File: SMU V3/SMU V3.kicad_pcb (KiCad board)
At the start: 4 copper layers, 55.5 x 74.8 mm, 86 parts, among them J1 Connector, J2 Connector, J3 SMA, J4 SMA, Q1 SI2301CDS-T1-GE3, U1 LSM6DSOTR, U2 TPS7A2033PDBVR, U3 TPS7A2033PDBVR, U4 TPS7A2033PDBVR, U5 ETQ-P3M150KVN, U6 TPS5430DDAR, U7 AMS1117-3.3

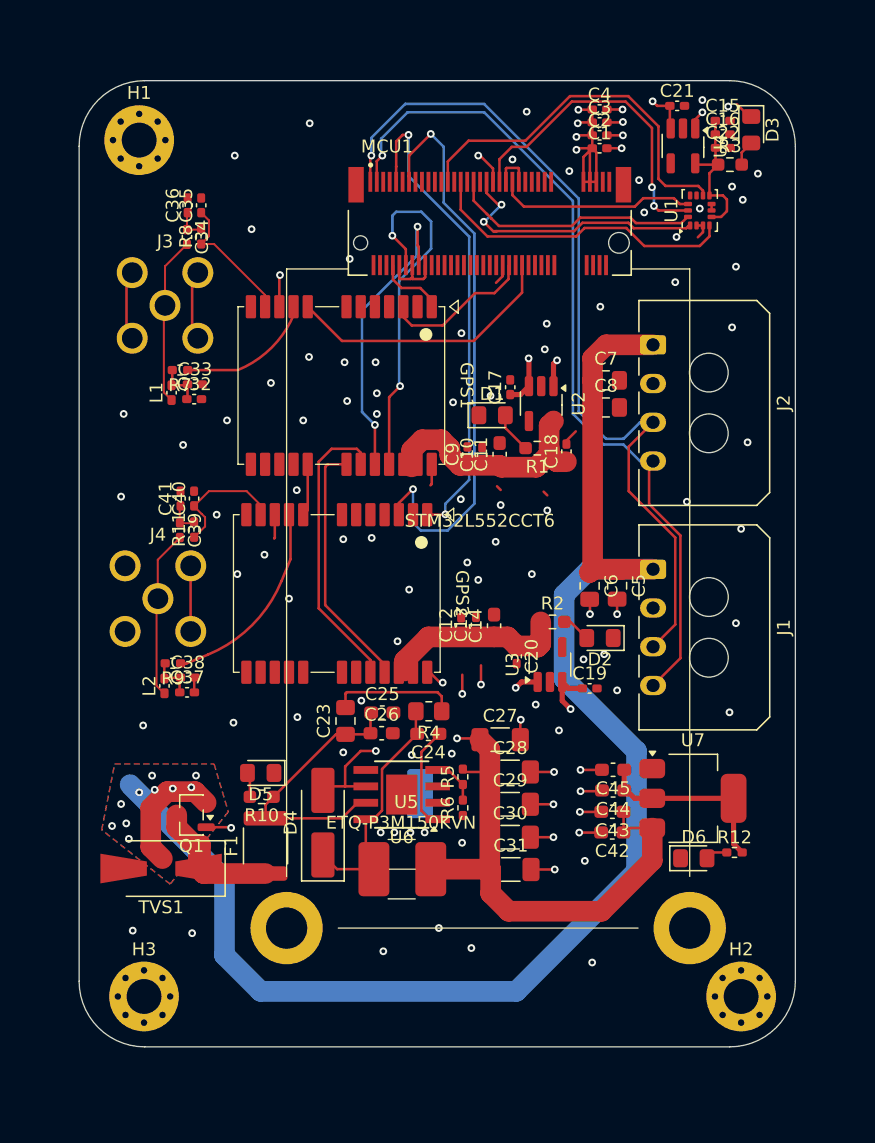
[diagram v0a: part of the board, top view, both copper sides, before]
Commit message: improved V3
added uart/spi test points and status leds
removed main 3v3 ldo
added silkscreen
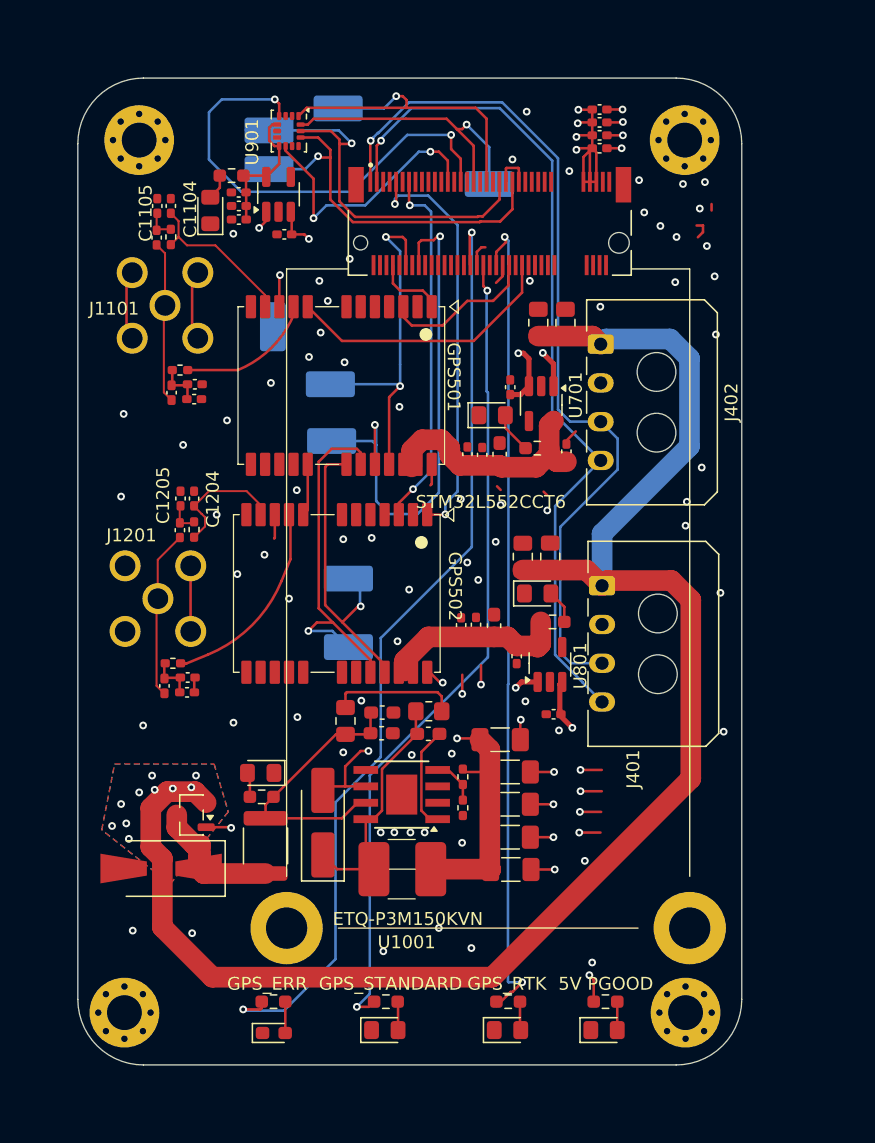
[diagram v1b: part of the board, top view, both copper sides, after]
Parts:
- removed C42, C43, C44, C45: 10u, Capacitor_SMD:C_0603_1608Metric_Pad1.08x0.95mm_HandSolder
- removed D6: Green, Diode_SMD:D_0805_2012Metric_Pad1.15x1.40mm_HandSolder
- removed R12: 220, Resistor_SMD:R_0402_1005Metric_Pad0.72x0.64mm_HandSolder
- removed U7: AMS1117-3.3, Package_TO_SOT_SMD:SOT-223-3_TabPin2
- added D101: Green, Diode_SMD:D_0805_2012Metric_Pad1.15x1.40mm_HandSolder, F.Cu at (165.1, 128.1)
- added D201: Green, Diode_SMD:D_0805_2012Metric_Pad1.15x1.40mm_HandSolder, F.Cu at (157.6, 128.1)
- added D202: Yellow, Diode_SMD:D_0805_2012Metric_Pad1.15x1.40mm_HandSolder, F.Cu at (148.1, 128.1)
- added D203: Red, Diode_SMD:D_0603_1608Metric_Pad1.05x0.95mm_HandSolder, F.Cu at (139.5, 128.3)
- added G***: LOGO, bfr_logos:BFR_Small, B.Cu at (134.6, 105.9)
- added G***: LOGO, images:smu_qrCode, B.Cu at (156.3, 117.3)
- added G***: LOGO, images:sleepingBubu_v2, B.Cu at (156.6, 83.6)
- added H104: MountingHole_Pad_MP, MountingHole:MountingHole_2.7mm_M2.5_Pad_Via, F.Cu at (171.3, 59.2)
- added R101: 120, Resistor_SMD:R_0603_1608Metric_Pad0.98x0.95mm_HandSolder, F.Cu at (165.2, 125.9)
- added R201: 120, Resistor_SMD:R_0603_1608Metric_Pad0.98x0.95mm_HandSolder, F.Cu at (157.7, 125.9)
- added R202: 120, Resistor_SMD:R_0603_1608Metric_Pad0.98x0.95mm_HandSolder, F.Cu at (148.2, 125.9)
- added R203: 120, Resistor_SMD:R_0603_1608Metric_Pad0.98x0.95mm_HandSolder, F.Cu at (139.5, 125.9)
- added TP501: GPS1_UART_RX, bfr_utilities:TestPoint_Keystone_5019_Miniature, B.Cu at (143.9, 78.1)
- added TP502: GPS1_UART_TX, bfr_utilities:TestPoint_Keystone_5019_Miniature, B.Cu at (144.0, 82.5)
- added TP503: GPS2_UART_RX, bfr_utilities:TestPoint_Keystone_5019_Miniature, B.Cu at (145.3, 93.2)
- added TP504: GPS2_UART_TX, bfr_utilities:TestPoint_Keystone_5019_Miniature, B.Cu at (145.3, 98.5)
- added TP601: IMU_SPI_CS, bfr_utilities:TestPoint_Keystone_5019_Miniature, B.Cu at (139.2, 61.5)
- added TP602: IMU_SPI_MISO, bfr_utilities:TestPoint_Keystone_5019_Miniature, B.Cu at (144.5, 56.8)
- added TP603: IMU_SPI_MOSI, bfr_utilities:TestPoint_Keystone_5019_Miniature, B.Cu at (156.2, 62.6)
- added TP604: IMU_SPI_SCK, bfr_utilities:TestPoint_Keystone_5019_Miniature, B.Cu at (139.2, 58.5)
- moved D901 42.3 mm to (134.6, 64.7), turned to 90 degrees
- moved R901 38.6 mm to (136.3, 62.0), turned to 180 degrees
- moved C601 38.2 mm to (136.8, 65.3), turned to 180 degrees
- moved TP301 37.9 mm to (139.4, 73.7)
- moved C602 37.9 mm to (136.8, 64.3), turned to 180 degrees
- moved C902 37.6 mm to (136.8, 63.2), turned to 180 degrees
- moved U601 32.4 mm to (140.7, 58.5), turned to -90 degrees
- moved C901 32.0 mm to (140.3, 66.5), turned to 180 degrees
- moved U901 31.5 mm to (139.9, 63.4), turned to 90 degrees
- moved C401 7.64 mm to (158.8, 91.5), turned to 90 degrees
- moved C404 7.28 mm to (162.1, 73.3), turned to 90 degrees
- moved C403 6.88 mm to (160.0, 73.3), turned to 90 degrees
- moved D801 5.93 mm to (159.9, 94.3), turned to 0 degrees
- moved H102 4.48 mm to (171.4, 126.8)
- moved J401 4.15 mm to (164.9, 93.7)
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- renumbered C23 to C1001, C24 to C1002, C25 to C1003, C26 to C1004, C27 to C1005, C28 to C1006, C29 to C1007, C30 to C1008, C31 to C1009, C32 to C1101, C33 to C1102, C34 to C1103, C35 to C1104, C36 to C1105, C37 to C1201, C38 to C1202, C39 to C1203, C40 to C1204, C41 to C1205, C1 to C201, C2 to C202, C3 to C203, C4 to C204, C5 to C401, C6 to C402, C7 to C403, C8 to C404, C9 to C501, C10 to C502, C11 to C503, C12 to C504, C13 to C505, C14 to C506, C15 to C601, C16 to C602, C17 to C701, C18 to C702, C19 to C801, C20 to C802, C21 to C901, C22 to C902, D4 to D1001, D5 to D1201, D1 to D701, D2 to D801, D3 to D901, F1 to F1201, GPS1 to GPS501, GPS2 to GPS502, H1 to H101, H2 to H102, H3 to H103, J3 to J1101, J4 to J1201, J1 to J401, J2 to J402, L1 to L1101, L2 to L1201, MCU1 to MCU201, Q1 to Q1201, R4 to R1001, R5 to R1002, R6 to R1003, R7 to R1101, R8 to R1102, R9 to R1201, R10 to R1202, R11 to R1203, R1 to R701, R2 to R801, R3 to R901, TP1 to TP301, TVS1 to TVS1201, U5 to U1001, U6 to U1002, U1 to U601, U2 to U701, U3 to U801, U4 to U901
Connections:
- MCU201 pad 28: /Microcontroller/DISP_I2C_SCL -> unconnected-(MCU201B-PB13-Pad28)
- MCU201 pad 32: unconnected-(MCU1B-PB12-Pad32) -> /Microcontroller/GPS_Error
- MCU201 pad 36: unconnected-(MCU1B-PB11-Pad36) -> /Microcontroller/GPS_Standard
- MCU201 pad 40: unconnected-(MCU1B-PB10-Pad40) -> /Microcontroller/GPS_RTK
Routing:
- net /Microcontroller/GPS_Error: track 0.00 -> 74.0 mm, vias 0 -> 2
- net /Microcontroller/GPS_RTK: track 0.00 -> 64.2 mm, vias 0 -> 2
- net /Microcontroller/GPS_Standard: track 0.00 -> 62.8 mm, vias 0 -> 2
- net +5V: track 75.2 -> 55.9 mm, vias 11 -> 12
- net /GPS1.UART_TX: track 23.6 -> 42.0 mm
- net /GPS2.PPS: track 45.3 -> 28.2 mm
- net +3V3: track 14.6 -> 0.00 mm
- net /IMU_SPI.CS: track 15.4 -> 29.1 mm, vias 0 -> 1
- net /IMU/IMU_INT1: track 24.3 -> 36.1 mm, vias 0 -> 2
- net GND: track 76.9 -> 66.5 mm, vias 104 -> 89
- net /IMU/IMU_INT2: track 29.2 -> 20.9 mm, vias 0 -> 2
- net /IMU_SPI.SCK: track 25.1 -> 32.5 mm, vias 2 -> 1
- net /GPS/GPS2.UART_TX: track 22.6 -> 28.4 mm, vias 0 -> 1
- net /GPS2.WKUP: track 37.8 -> 32.3 mm
- net /IMU_SPI.MISO: track 21.1 -> 26.5 mm, vias 2 -> 1
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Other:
- board size 55.5 x 74.8 mm -> 51.4 x 76.4 mm
- board text added: "5V PGOOD"
- board text added: "GND"
- board text added: "GPS1_UART_RX"
- board text added: "GPS_ERR"
- board text added: "GPS_RTK"
- board text added: "GPS_STANDARD"
- board text added: "Spatial Monitoring Unit"

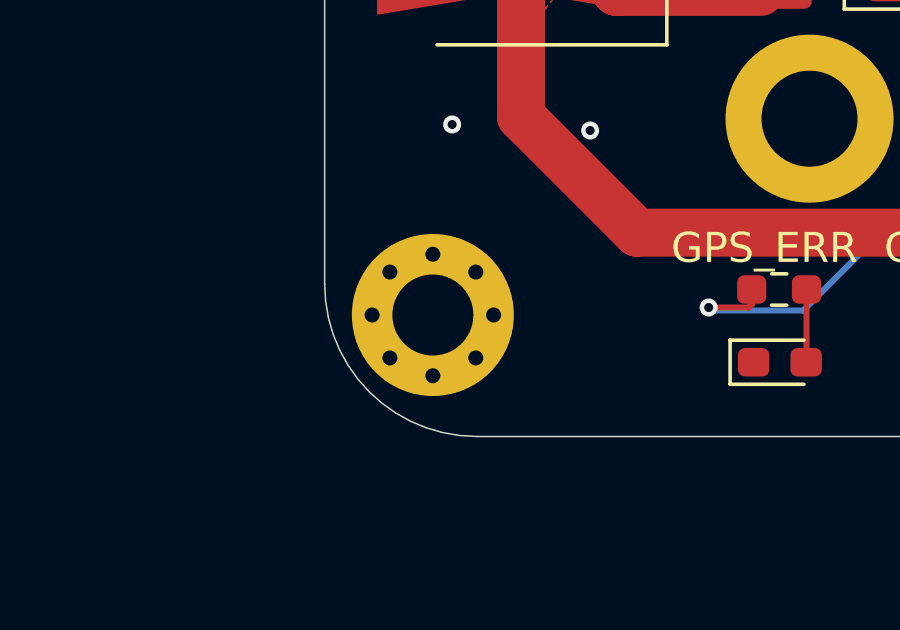
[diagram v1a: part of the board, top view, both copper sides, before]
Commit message: fixed mounting holes
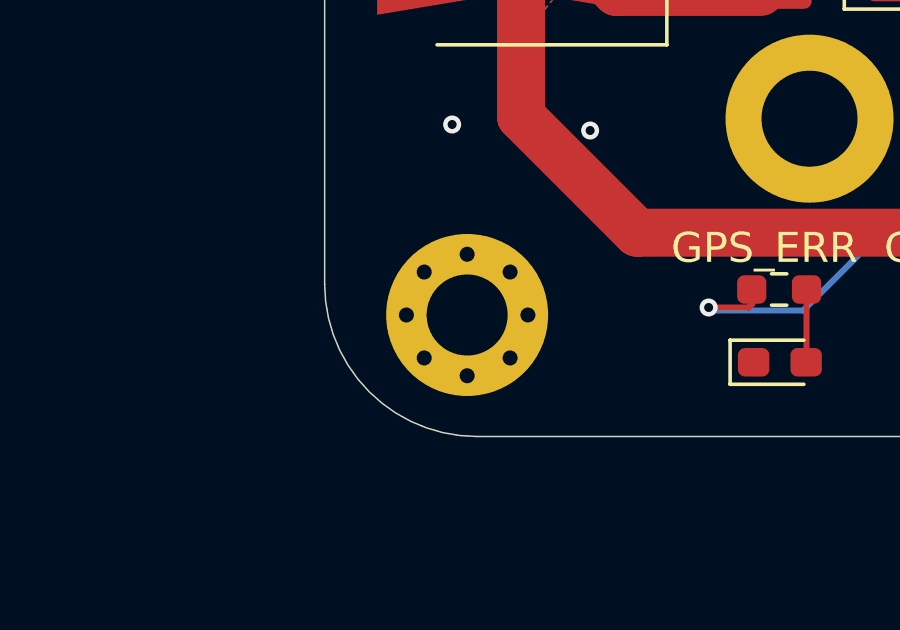
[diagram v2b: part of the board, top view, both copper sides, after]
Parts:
- moved H103 1.14 mm to (129.1, 126.8)
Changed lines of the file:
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@@
 	(footprint "MountingHole:MountingHole_2.7mm_M2.5_Pad_Via"
 		(layer "F.Cu")
-		(at 127.956891 126.75)
+		(at 129.1 126.75)
 		(descr "Mounting Hole 2.7mm, M2.5, generated by kicad-footprint-generator mountinghole.py")
 		(tags "mountinghole M2.5")

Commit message: actual final v3
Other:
- board text added: "C1001"
- board text added: "F1201"
- board text added: "TVS1201"
- board text added: "U601"
